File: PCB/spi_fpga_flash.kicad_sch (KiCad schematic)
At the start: 6 parts, among them U3 XC7A100T-FTG256, U4 IS25WP256D-xM

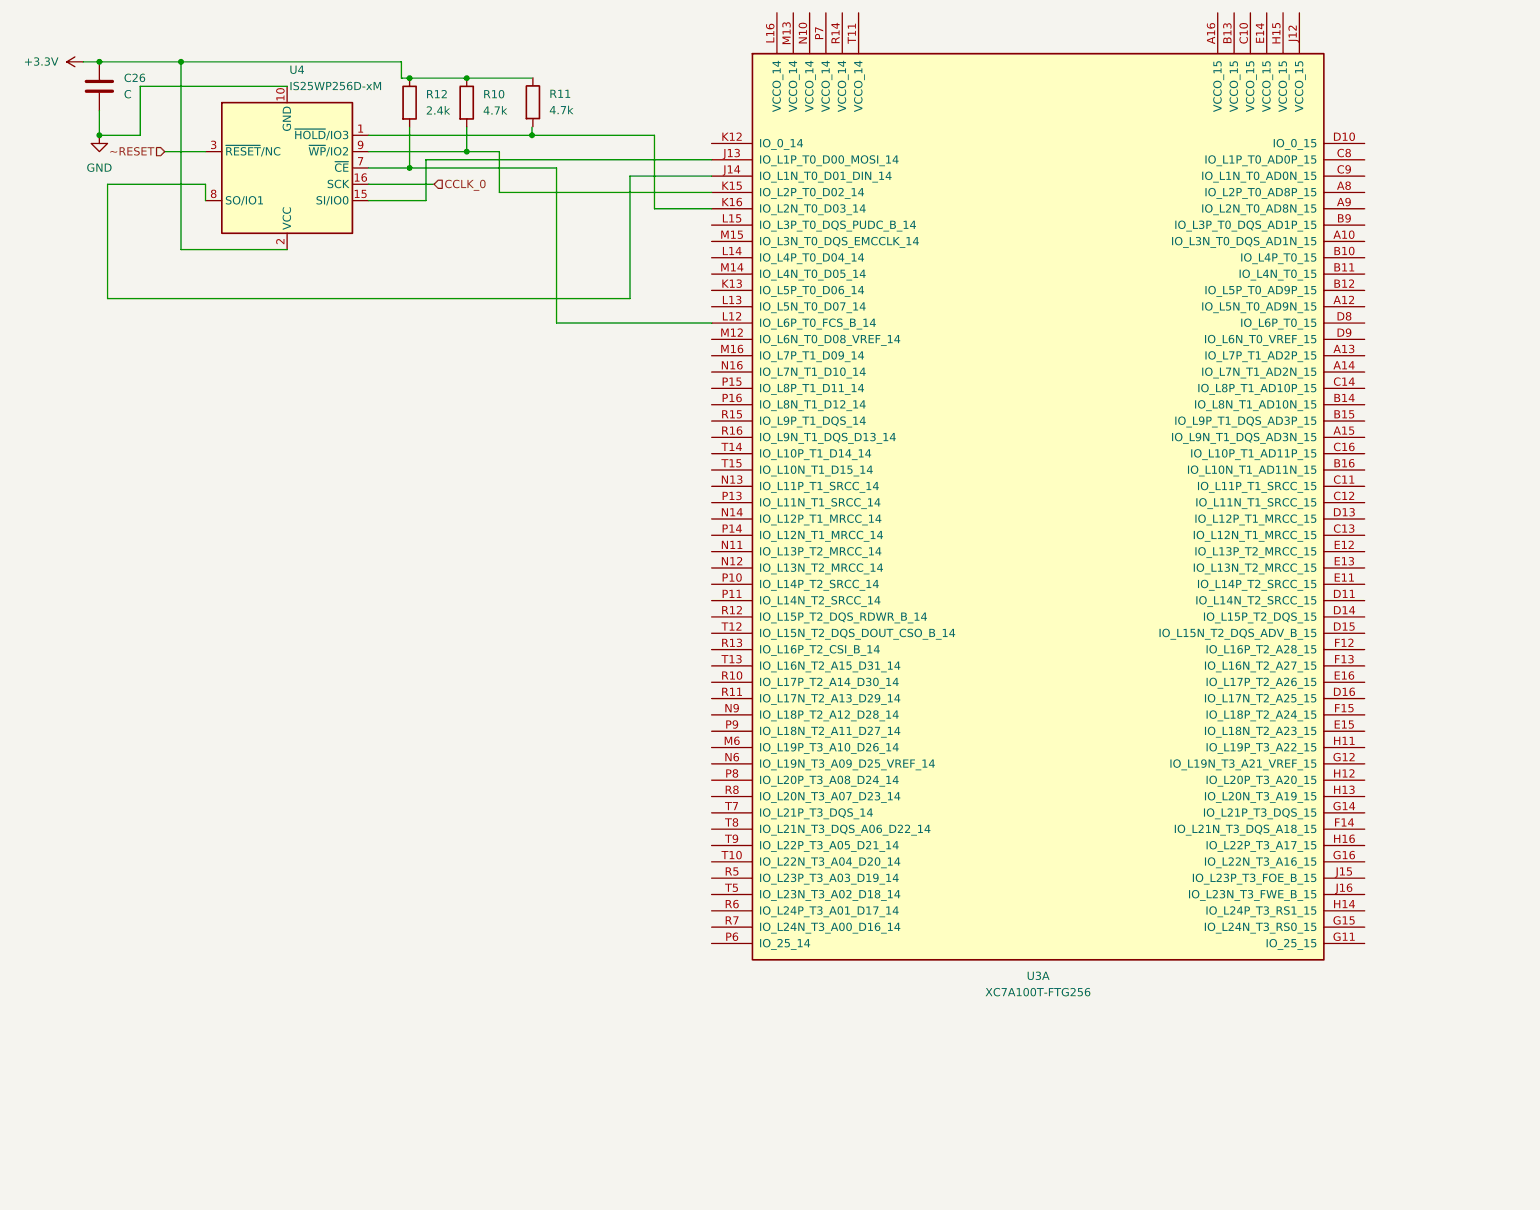
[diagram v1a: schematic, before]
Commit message: pcb: cleanup mcu sram (#10)
Co-authored-by: Kolbjørn Austreng <kolbjorn.austreng@hotzen.io>
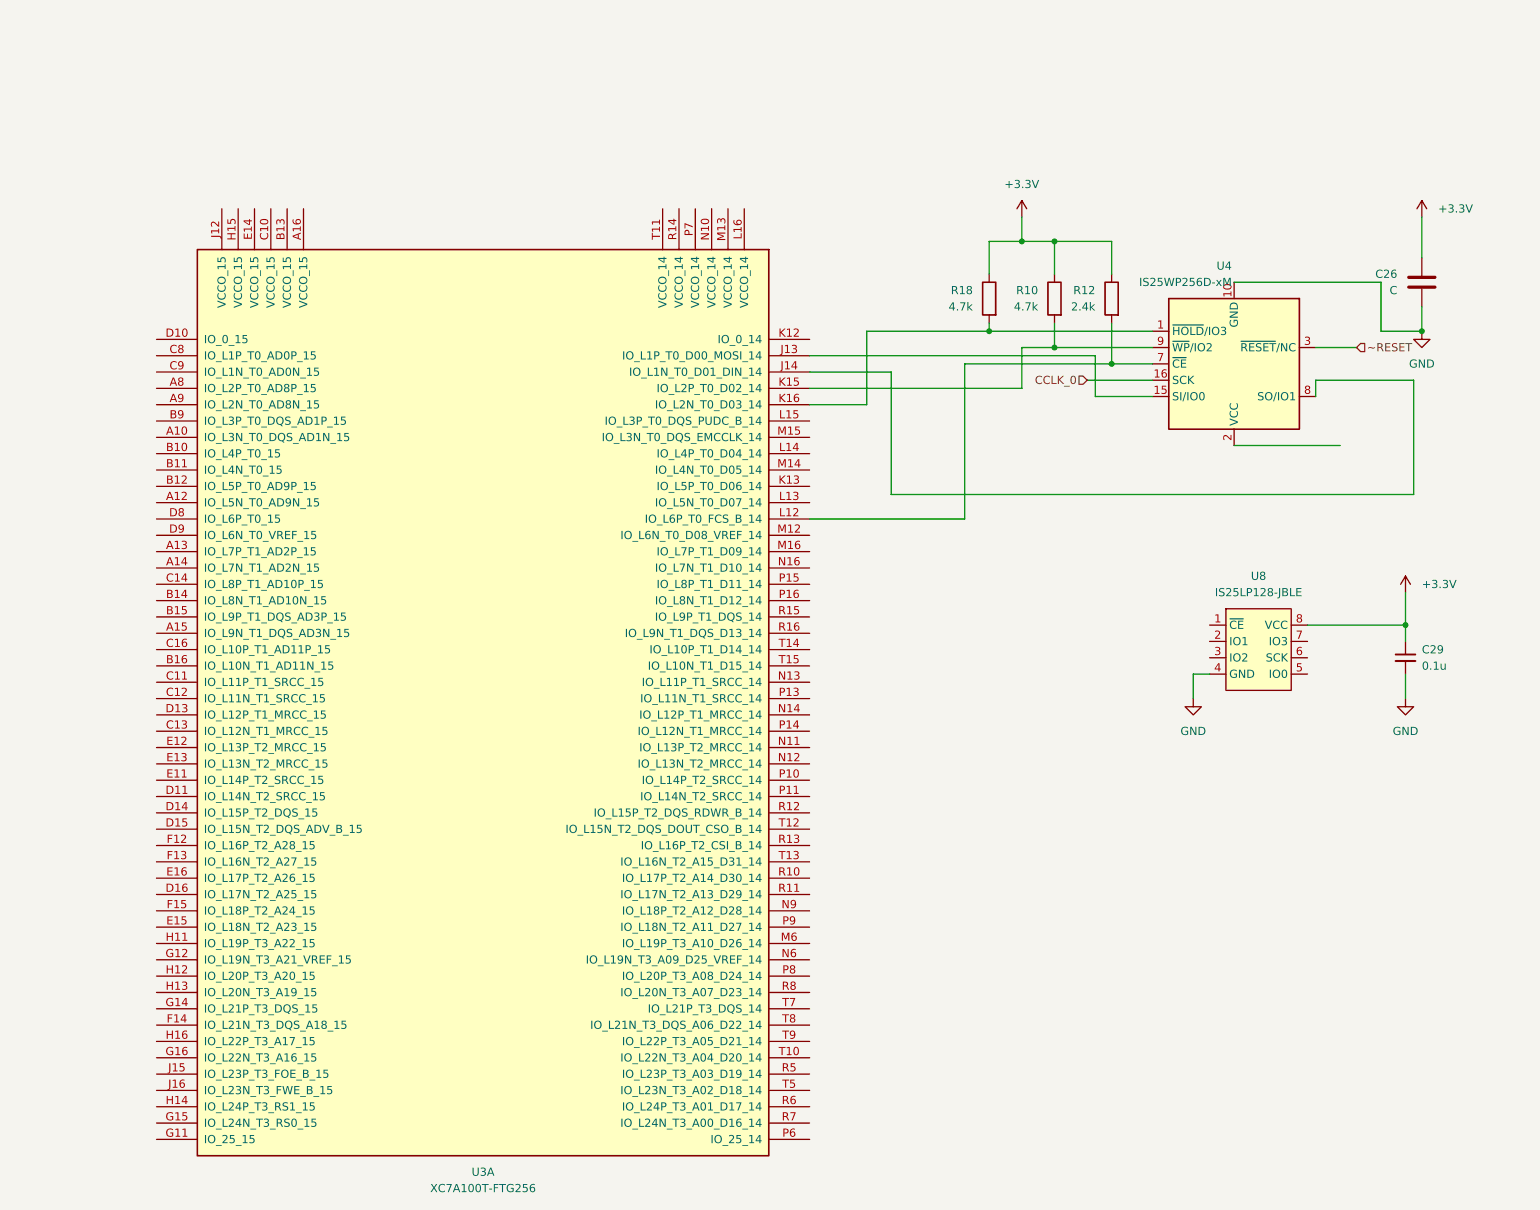
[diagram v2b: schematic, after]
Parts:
- removed R11: 4.7k, symbol Device:R
- added C29: 0.1u, symbol Device:C_Small
- added R18: 4.7k, symbol Device:R
- added U8: IS25LP128-JBLE, symbol 0000_CustomComponents:IS25LP128-JBLE
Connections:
- net +3.3V: now also C29.1, R18.1, U8.8 (VCC); no longer U4.2 (VCC)
- net GND: now also C29.2, U8.4 (GND)
- net at U3.K16 (IO_L2N_T0_D03_14), U4.1 (~{HOLD}/IO3): now also R18.2
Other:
- moved on the sheet: C26, R10, R12, U3A, U4

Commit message: dump
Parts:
- added C? (x4): 470nF, Capacitor_SMD:C_0603_1608Metric_Pad1.08x0.95mm_HandSolder, symbol Device:C
- added C? (x2): 4.7uF, Capacitor_SMD:C_0805_2012Metric_Pad1.18x1.45mm_HandSolder, symbol Device:C
- added C?: 47uF, Capacitor_SMD:C_1210_3225Metric_Pad1.33x2.70mm_HandSolder, symbol Device:C
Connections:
- net GND: now also U4.2 (VCC), C?.2, C?.2, C?.2, C?.2, C?.2, C?.2, C?.2
- net +3V3: now reaches U3.L16 (VCCO_14)
- net +3V3: now also U3.M13 (VCCO_14), U3.N10 (VCCO_14), U3.P7 (VCCO_14), U3.R14 (VCCO_14), U3.T11 (VCCO_14), C?.1, C?.1, C?.1, C?.1, C?.1, C?.1, C?.1
